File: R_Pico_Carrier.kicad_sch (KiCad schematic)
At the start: 30 parts, among them J1 Conn_01x03_Pin, J2 Conn_01x08_Pin, J3 Conn_01x01_Pin, J4 Conn_01x01_Pin, J5 Conn_01x01_Pin, J6 Conn_01x01_Pin, J7 Conn_01x01_Pin, J8 Conn_01x01_Pin, U1 MCP73831-2-OT, U4 CH32V003FxUx

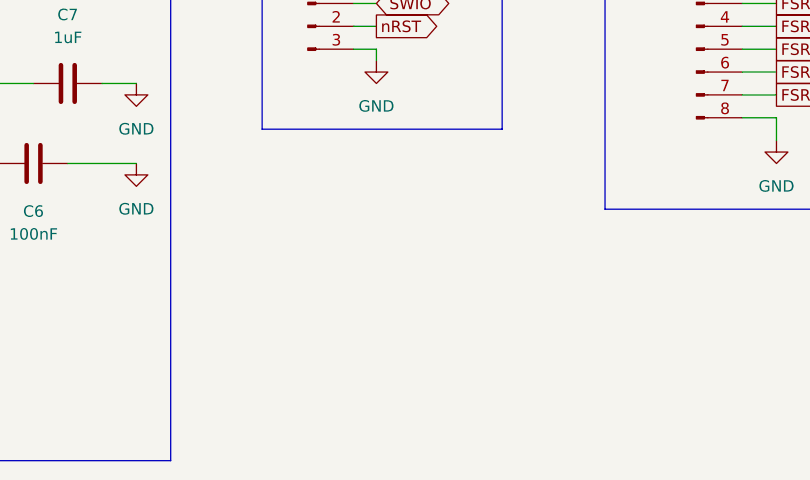
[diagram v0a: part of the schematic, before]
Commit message: Re-do the board for smaller and tidy palcement
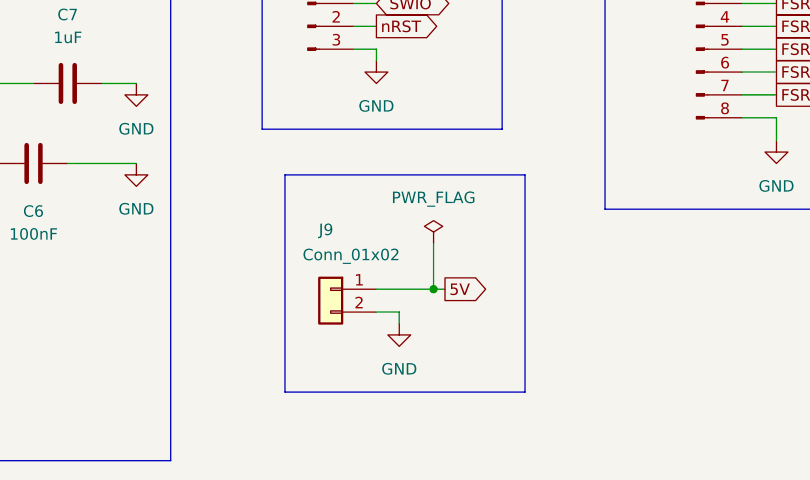
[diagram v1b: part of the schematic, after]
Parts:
- added J9: Conn_01x02, Connector_PinHeader_2.54mm:PinHeader_1x02_P2.54mm_Vertical, symbol Connector_Generic:Conn_01x02
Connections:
- net 5V: now also J9.1 (Pin_1)
- net GND: now also J9.2 (Pin_2)
